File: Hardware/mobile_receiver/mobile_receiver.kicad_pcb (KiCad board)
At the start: 4 copper layers, 82.5 x 142 mm, 33 parts, among them J1 Conn_02x07_Top_Bottom, SW1 SW_SPST, SW2 SW_Push, SW3 SW_Push, SW4 SW_Push, SW5 SW_Push, SW6 SW_Push, SW7 SW_Push, U2 kb2040

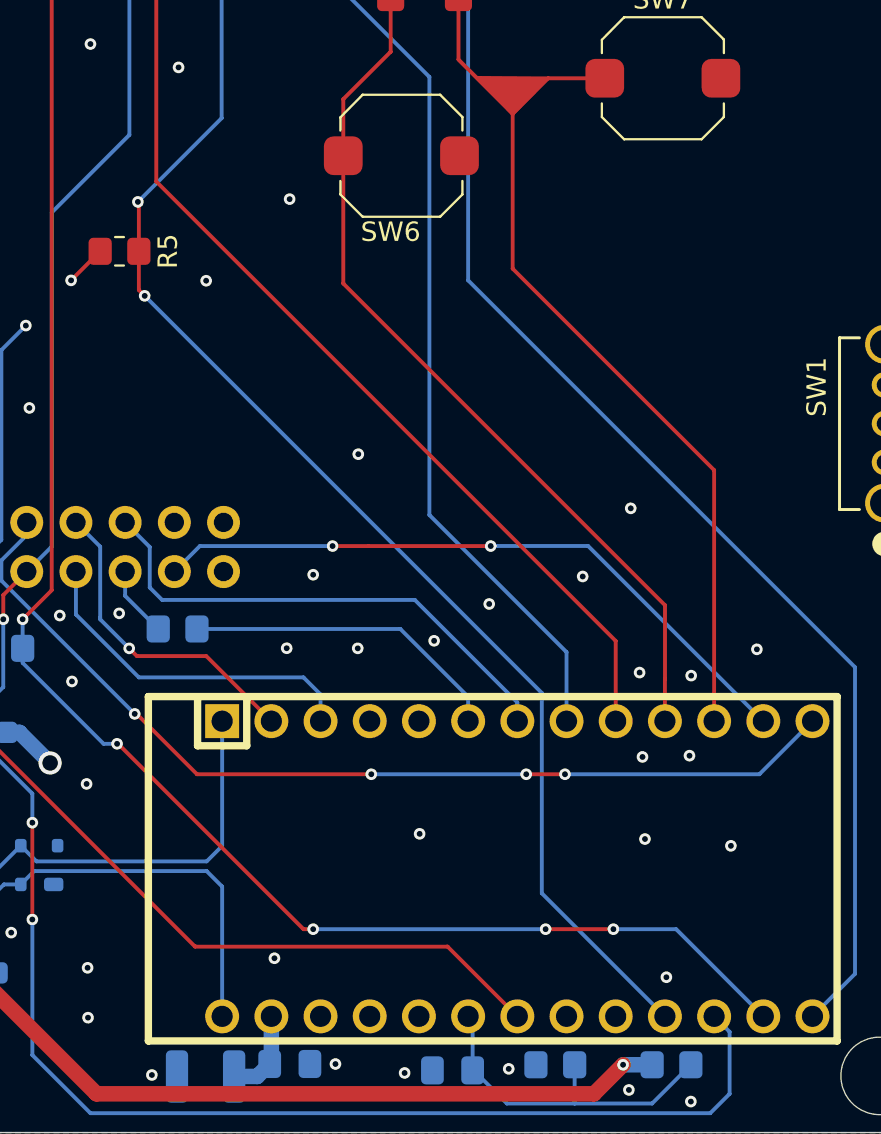
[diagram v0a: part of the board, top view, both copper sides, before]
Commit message: Vias and trace spacing
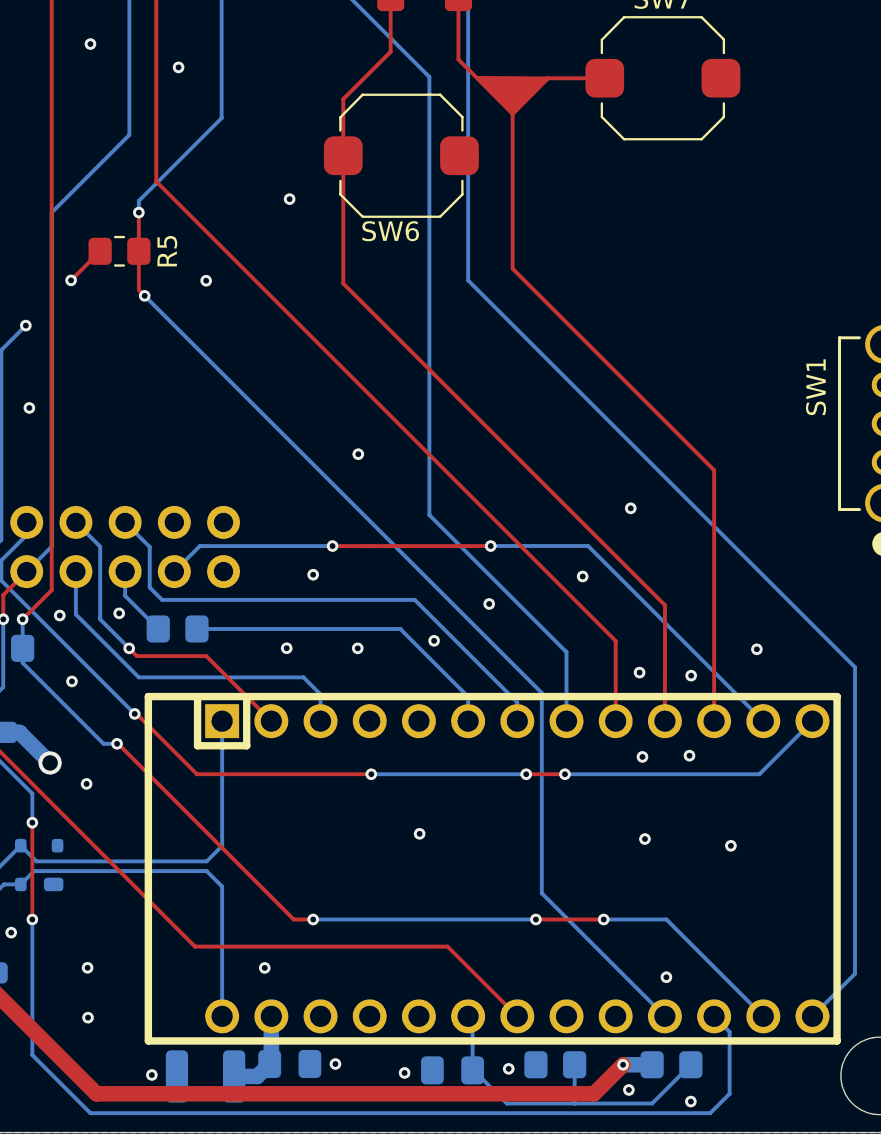
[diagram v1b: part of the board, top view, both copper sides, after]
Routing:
- added copper zone on In1.Cu, net GND
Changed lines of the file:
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@@
 	)
 	(via
-		(at 214.5 213)
+		(at 214 213.5)
 		(size 0.6)
 		(drill 0.3)
@@
 	)
 	(segment
-		(start 216 211.5)
-		(end 206.43 201.93)
+		(start 206.43 201.93)
+		(end 206.375 201.93)
+		(width 0.2)
+		(layer "F.Cu")
+		(net 18)
+	)
+	(segment
+		(start 231.5 211)
+		(end 228 211)
+		(width 0.2)
+		(layer "F.Cu")
+		(net 18)
+	)
+	(segment
+		(start 216.5 211)
+		(end 215.5 211)
 		(width 0.2)
 		(layer "F.Cu")
@@
 	)
 	(segment
-		(start 216.5 211.5)
-		(end 216 211.5)
+		(start 215.5 211)
+		(end 206.43 201.93)
 		(width 0.2)
 		(layer "F.Cu")
 		(net 18)
 	)
-	(segment
-		(start 206.43 201.93)
-		(end 206.375 201.93)
-		(width 0.2)
-		(layer "F.Cu")
+	(via
+		(at 231.5 211)
+		(size 0.6)
+		(drill 0.3)
+		(layers "F.Cu" "B.Cu")
 		(net 18)
 	)
-	(segment
-		(start 228.5 211.5)
-		(end 232 211.5)
-		(width 0.2)
-		(layer "F.Cu")
+	(via
+		(at 203 144)
+		(size 0.6)
+		(drill 0.3)
+		(layers "F.Cu" "B.Cu")
 		(net 18)
 	)
 	(via
-		(at 232 211.5)
+		(at 228 211)
 		(size 0.6)
 		(drill 0.3)
@@
 	)
 	(via
-		(at 203 144)
+		(at 201.5 195.5)
 		(size 0.6)
 		(drill 0.3)
@@
 	)
 	(via
-		(at 228.5 211.5)
-		(size 0.6)
-		(drill 0.3)
-		(layers "F.Cu" "B.Cu")
-		(net 18)
-	)
-	(via
-		(at 201.5 195.5)
-		(size 0.6)
-		(drill 0.3)
-		(layers "F.Cu" "B.Cu")
-		(net 18)
-	)
-	(via
-		(at 216.5 211.5)
+		(at 216.5 211)
 		(size 0.6)
 		(drill 0.3)
@@
 	)
 	(segment
-		(start 216.5 211.5)
-		(end 228.5 211.5)
-		(width 0.2)
-		(layer "B.Cu")
-		(net 18)
-	)
-	(segment
-		(start 232 211.5)
-		(end 235.24 211.5)
-		(width 0.2)
-		(layer "B.Cu")
-		(net 18)
-	)
-	(segment
 		(start 201.5 197)
 		(end 201.5 195.5)
@@
 	)
 	(segment
-		(start 235.24 211.5)
-		(end 239.74 216)
+		(start 228 211)
+		(end 216.5 211)
 		(width 0.2)
 		(layer "B.Cu")
@@
 	)
 	(segment
+		(start 234.74 211)
+		(end 239.74 216)
+		(width 0.2)
+		(layer "B.Cu")
+		(net 18)
+	)
+	(segment
 		(start 203 144)
 		(end 203 137.583047)
@@
 	)
 	(segment
+		(start 231.5 211)
+		(end 234.74 211)
+		(width 0.2)
+		(layer "B.Cu")
+		(net 18)
+	)
+	(segment
 		(start 207.5 178.5)
 		(end 207.5 176.5)
@@
 	)
 	(segment
-		(start 207.45 173.95)
-		(end 207.5 174)
+		(start 207.5 174.5)
+		(end 207.5 176.5)
 		(width 0.2)
 		(layer "F.Cu")
@@
 		(net 19)
 	)
-	(segment
-		(start 207.5 174)
-		(end 207.5 176.5)
-		(width 0.2)
-		(layer "F.Cu")
+	(via
+		(at 207.8 178.8)
+		(size 0.6)
+		(drill 0.3)
+		(layers "F.Cu" "B.Cu")
 		(net 19)
 	)
 	(via
-		(at 207.8 178.8)
+		(at 207.5 174.5)
 		(size 0.6)
 		(drill 0.3)
@@
 		(net 19)
 	)
-	(via
-		(at 207.45 173.95)
-		(size 0.6)
-		(drill 0.3)
-		(layers "F.Cu" "B.Cu")
+	(segment
+		(start 207.5 174.5)
+		(end 207.5 173.9)
+		(width 0.2)
+		(layer "B.Cu")
 		(net 19)
 	)
@@
 	)
 	(segment
+		(start 228.304781 209.644781)
+		(end 234.66 216)
+		(width 0.2)
+		(layer "B.Cu")
+		(net 19)
+	)
+	(segment
+		(start 207.5 173.9)
+		(end 211.774427 169.625573)
+		(width 0.2)
+		(layer "B.Cu")
+		(net 19)
+	)
+	(segment
+		(start 211.774427 133.88862)
+		(end 212.884427 132.77862)
+		(width 0.2)
+		(layer "B.Cu")
+		(net 19)
+	)
+	(segment
 		(start 211.774427 169.625573)
 		(end 211.774427 133.88862)
-		(width 0.2)
-		(layer "B.Cu")
-		(net 19)
-	)
-	(segment
-		(start 228.304781 209.644781)
-		(end 234.66 216)
-		(width 0.2)
-		(layer "B.Cu")
-		(net 19)
-	)
-	(segment
-		(start 211.774427 133.88862)
-		(end 212.884427 132.77862)
-		(width 0.2)
-		(layer "B.Cu")
-		(net 19)
-	)
-	(segment
-		(start 207.45 173.95)
-		(end 211.774427 169.625573)
 		(width 0.2)
 		(layer "B.Cu")
@@
 		(connect_pads
 			(clearance 0.5)
+		)
+		(min_thickness 0.25)
+		(filled_areas_thickness no)
+		(fill yes
+			(thermal_gap 0.5)
+			(thermal_bridge_width 0.5)
+		)
+		(polygon
+			(pts
+				(xy 166.5 80) (xy 249 80) (xy 249 222) (xy 166.5 222)
+			)
+		)
+	)
+	(zone
+		(net 1)
+		(net_name "GND")
+		(layer "In1.Cu")
+		(hatch edge 0.5)
+		(connect_pads
+			(clearance 0.5)

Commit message: Saved the previous update in kicad
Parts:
- C3, C6: footprint Capacitor_SMD:C_1210_3225Metric -> Capacitor_SMD:C_0805_2012Metric_Pad1.18x1.45mm_HandSolder
- moved C3 0.46 mm to (192.5, 194.0)
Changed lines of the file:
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@@
 		)
 	)
-	(footprint "Capacitor_SMD:C_1210_3225Metric"
+	(footprint "Capacitor_SMD:C_0805_2012Metric_Pad1.18x1.45mm_HandSolder"
 		(layer "B.Cu")
-		(at 192.5 194.5 90)
-		(descr "Capacitor SMD 1210 (3225 Metric), square (rectangular) end terminal, IPC-7351 nominal, (Body size source: IPC-SM-782 page 76, https://www.pcb-3d.com/wordpress/wp-content/uploads/ipc-sm-782a_amendment_1_and_2.pdf), generated with kicad-footprint-generator")
-		(tags "capacitor")
+		(at 192.5 194.0375 90)
+		(descr "Capacitor SMD 0805 (2012 Metric), square (rectangular) end terminal, IPC-7351 nominal with elongated pad for handsoldering. (Body size source: IPC-SM-782 page 76, https://www.pcb-3d.com/wordpress/wp-content/uploads/ipc-sm-782a_amendment_1_and_2.pdf, https://docs.google.com/spreadsheets/d/1BsfQQcO9C6DZCsRaXUlFlo91Tg2WpOkGARC1WS5S8t0/edit?usp=sharing), generated with kicad-footprint-generator")
+		(tags "capacitor handsolder")
 		(property "Reference" "C3"
-			(at 0 -2.5 270)
+			(at -0.4625 1.68 270)
 			(layer "B.SilkS")
 			(effects
@@
 		)
 		(property "Value" "10uF"
-			(at 0 -2.3 90)
+			(at 0 -1.68 270)
 			(layer "B.Fab")
 			(effects
@@
 		)
 		(property "Datasheet" "~"
-			(at 0 0 90)
+			(at 0 0 270)
 			(layer "B.Fab")
 			(hide yes)
@@
 		)
 		(property "Description" "Unpolarized capacitor"
-			(at 0 0 90)
+			(at 0 0 270)
 			(layer "B.Fab")
 			(hide yes)
@@
 		(attr smd)
 		(fp_line
-			(start -0.711252 -1.36)
-			(end 0.711252 -1.36)
+			(start -0.261252 -0.735)
+			(end 0.261252 -0.735)
 			(stroke
 				(width 0.12)
@@
 		)
 		(fp_line
-			(start -0.711252 1.36)
-			(end 0.711252 1.36)
+			(start -0.261252 0.735)
+			(end 0.261252 0.735)
 			(stroke
 				(width 0.12)
@@
 		)
 		(fp_rect
-			(start -2.3 1.6)
-			(end 2.3 -1.6)
+			(start -1.88 0.98)
+			(end 1.88 -0.98)
 			(stroke
 				(width 0.05)
@@
 		)
 		(fp_rect
-			(start -1.6 1.25)
-			(end 1.6 -1.25)
+			(start -1 0.625)
+			(end 1 -0.625)
 			(stroke
 				(width 0.1)
@@
 		)
 		(fp_text user "${REFERENCE}"
-			(at 0 0 90)
+			(at 0 0 270)
 			(layer "B.Fab")
 			(effects
 				(font
-					(size 0.8 0.8)
-					(thickness 0.12)
+					(size 0.5 0.5)
+					(thickness 0.08)
 				)
 				(justify mirror)
@@
 		)
 		(pad "1" smd roundrect
-			(at -1.475 0 90)
-			(size 1.15 2.7)
+			(at -1.0375 0 90)
+			(size 1.175 1.45)
 			(layers "B.Cu" "B.Mask" "B.Paste")
-			(roundrect_rratio 0.217391)
+			(roundrect_rratio 0.212766)
 			(net 1 "GND")
 			(pintype "passive")
 		)
 		(pad "2" smd roundrect
-			(at 1.475 0 90)
-			(size 1.15 2.7)
+			(at 1.0375 0 90)
+			(size 1.175 1.45)
 			(layers "B.Cu" "B.Mask" "B.Paste")
-			(roundrect_rratio 0.217391)
+			(roundrect_rratio 0.212766)
 			(net 34 "+3.3V")
 			(pintype "passive")
 		)
 		(embedded_fonts no)
-		(model "${KICAD9_3DMODEL_DIR}/Capacitor_SMD.3dshapes/C_1210_3225Metric.step"
+		(model "${KICAD9_3DMODEL_DIR}/Capacitor_SMD.3dshapes/C_0805_2012Metric.step"
 			(offset
 				(xyz 0 0 0)
@@
 		)
 	)
-	(footprint "Capacitor_SMD:C_1210_3225Metric"
+	(footprint "Capacitor_SMD:C_0805_2012Metric_Pad1.18x1.45mm_HandSolder"
 		(layer "B.Cu")
 		(at 210.942559 219.105205 180)
-		(descr "Capacitor SMD 1210 (3225 Metric), square (rectangular) end terminal, IPC-7351 nominal, (Body size source: IPC-SM-782 page 76, https://www.pcb-3d.com/wordpress/wp-content/uploads/ipc-sm-782a_amendment_1_and_2.pdf), generated with kicad-footprint-generator")
-		(tags "capacitor")
+		(descr "Capacitor SMD 0805 (2012 Metric), square (rectangular) end terminal, IPC-7351 nominal with elongated pad for handsoldering. (Body size source: IPC-SM-782 page 76, https://www.pcb-3d.com/wordpress/wp-content/uploads/ipc-sm-782a_amendment_1_and_2.pdf, https://docs.google.com/spreadsheets/d/1BsfQQcO9C6DZCsRaXUlFlo91Tg2WpOkGARC1WS5S8t0/edit?usp=sharing), generated with kicad-footprint-generator")
+		(tags "capacitor handsolder")
 		(property "Reference" "C6"
-			(at 4.442559 0.105205 0)
+			(at 0 1.68 0)
 			(layer "B.SilkS")
 			(effects
@@
 		)
 		(property "Value" "4.7µF"
-			(at 0 -2.3 0)
+			(at 0 -1.68 0)
 			(layer "B.Fab")
-			(hide yes)
 			(effects
 				(font
@@
 		(attr smd)
 		(fp_line
-			(start -0.711252 1.36)
-			(end 0.711252 1.36)
+			(start -0.261252 0.735)
+			(end 0.261252 0.735)
 			(stroke
 				(width 0.12)
@@
 		)
 		(fp_line
-			(start -0.711252 -1.36)
-			(end 0.711252 -1.36)
+			(start -0.261252 -0.735)
+			(end 0.261252 -0.735)
 			(stroke
 				(width 0.12)
@@
 		)
 		(fp_rect
-			(start -2.3 1.6)
-			(end 2.3 -1.6)
+			(start -1.88 0.98)
+			(end 1.88 -0.98)
 			(stroke
 				(width 0.05)
@@
 		)
 		(fp_rect
-			(start -1.6 1.25)
-			(end 1.6 -1.25)
+			(start -1 0.625)
+			(end 1 -0.625)
 			(stroke
 				(width 0.1)
@@
 			(effects
 				(font
-					(size 0.8 0.8)
-					(thickness 0.12)
+					(size 0.5 0.5)
+					(thickness 0.08)
 				)
 				(justify mirror)
@@
 		)
 		(pad "1" smd roundrect
-			(at -1.475 0 180)
-			(size 1.15 2.7)
+			(at -1.0375 0 180)
+			(size 1.175 1.45)
 			(layers "B.Cu" "B.Mask" "B.Paste")
-			(roundrect_rratio 0.217391)
+			(roundrect_rratio 0.212766)
 			(net 4 "/SYS_VBUS")
 			(pintype "passive")
 		)
 		(pad "2" smd roundrect
-			(at 1.475 0 180)
-			(size 1.15 2.7)
+			(at 1.0375 0 180)
+			(size 1.175 1.45)
 			(layers "B.Cu" "B.Mask" "B.Paste")
-			(roundrect_rratio 0.217391)
+			(roundrect_rratio 0.212766)
 			(net 1 "GND")
 			(pintype "passive")
 		)
 		(embedded_fonts no)
-		(model "${KICAD9_3DMODEL_DIR}/Capacitor_SMD.3dshapes/C_1210_3225Metric.step"
+		(model "${KICAD9_3DMODEL_DIR}/Capacitor_SMD.3dshapes/C_0805_2012Metric.step"
 			(offset
 				(xyz 0 0 0)
@@
 	)
 	(via
-		(at 230.41493 193.289583)
+		(at 227.960154 189.922244)
 		(size 0.6)
 		(drill 0.3)
@@
 	)
 	(segment
-		(start 216 198.5)
-		(end 216.88 199.38)
+		(start 216.88 199.38)
+		(end 216.88 200.76)
 		(width 0.2)
 		(layer "B.Cu")
@@
 	)
 	(segment
-		(start 204.250805 195.250805)
-		(end 207.5 198.5)
+		(start 204.250805 195.599068)
+		(end 207.510509 198.858772)
 		(width 0.2)
 		(layer "B.Cu")
@@
 	)
 	(segment
-		(start 207.5 198.5)
-		(end 216 198.5)
+		(start 216.358772 198.858772)
+		(end 216.88 199.38)
 		(width 0.2)
 		(layer "B.Cu")
@@
 	)
 	(segment
-		(start 204.250805 193.037019)
-		(end 204.250805 195.250805)
+		(start 207.510509 198.858772)
+		(end 216.358772 198.858772)
 		(width 0.2)
 		(layer "B.Cu")
@@
 	)
 	(segment
-		(start 216.88 199.38)
-		(end 216.88 200.76)
+		(start 204.250805 193.037019)
+		(end 204.250805 195.599068)
 		(width 0.2)
 		(layer "B.Cu")
@@
 	)
 	(segment
-		(start 232.12 200.76)
-		(end 232.12 196.62)
+		(start 208.4 135.914193)
+		(end 205.264427 132.77862)
 		(width 0.2)
 		(layer "F.Cu")
@@
 	)
 	(segment
-		(start 208.4 135.914193)
-		(end 205.264427 132.77862)
+		(start 232.12 200.76)
+		(end 232.12 195.951903)
 		(width 0.2)
 		(layer "F.Cu")
@@
 	)
 	(segment
-		(start 208.4 172.9)
-		(end 208.4 135.914193)
+		(start 232.12 195.951903)
+		(end 208.4 172.231903)
 		(width 0.2)
 		(layer "F.Cu")
@@
 	)
 	(segment
-		(start 232.12 196.62)
-		(end 208.4 172.9)
+		(start 208.4 172.231903)
+		(end 208.4 135.914193)
 		(width 0.2)
 		(layer "F.Cu")

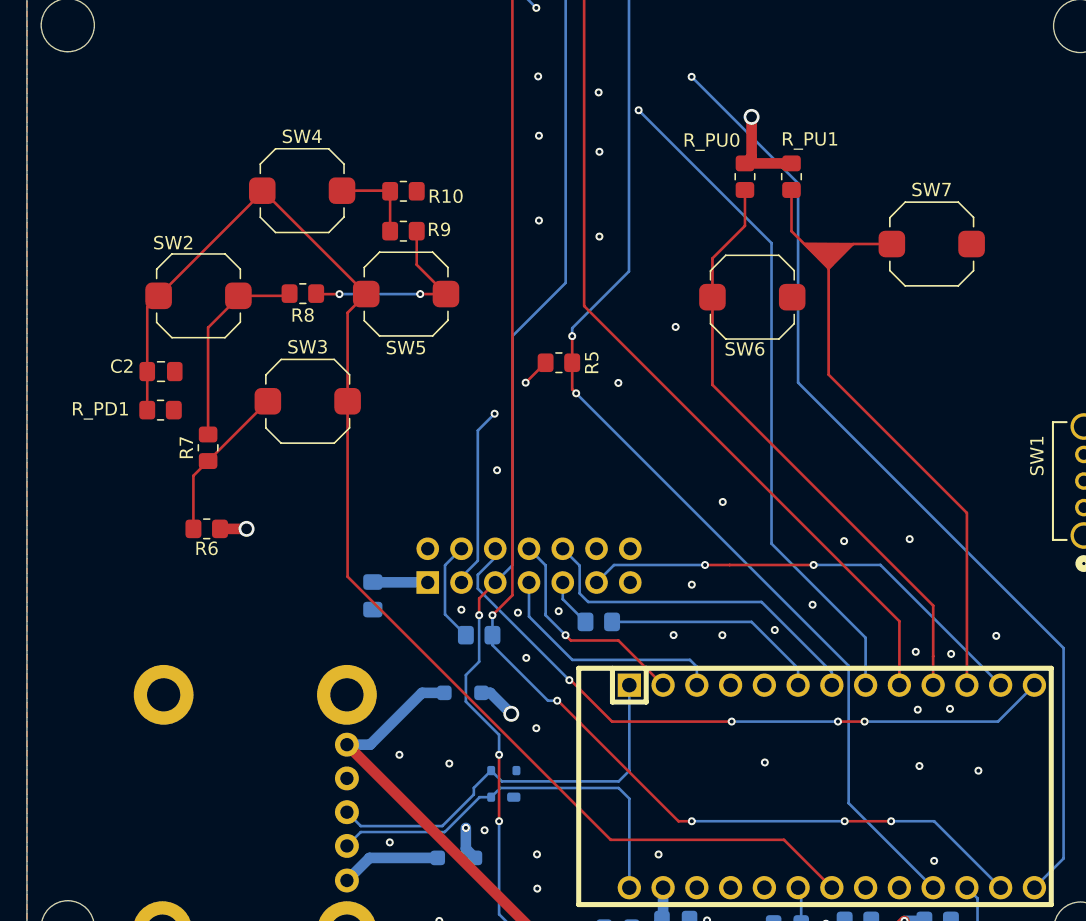
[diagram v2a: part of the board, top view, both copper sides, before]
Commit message: Updated traces and vias according to new switches and passives
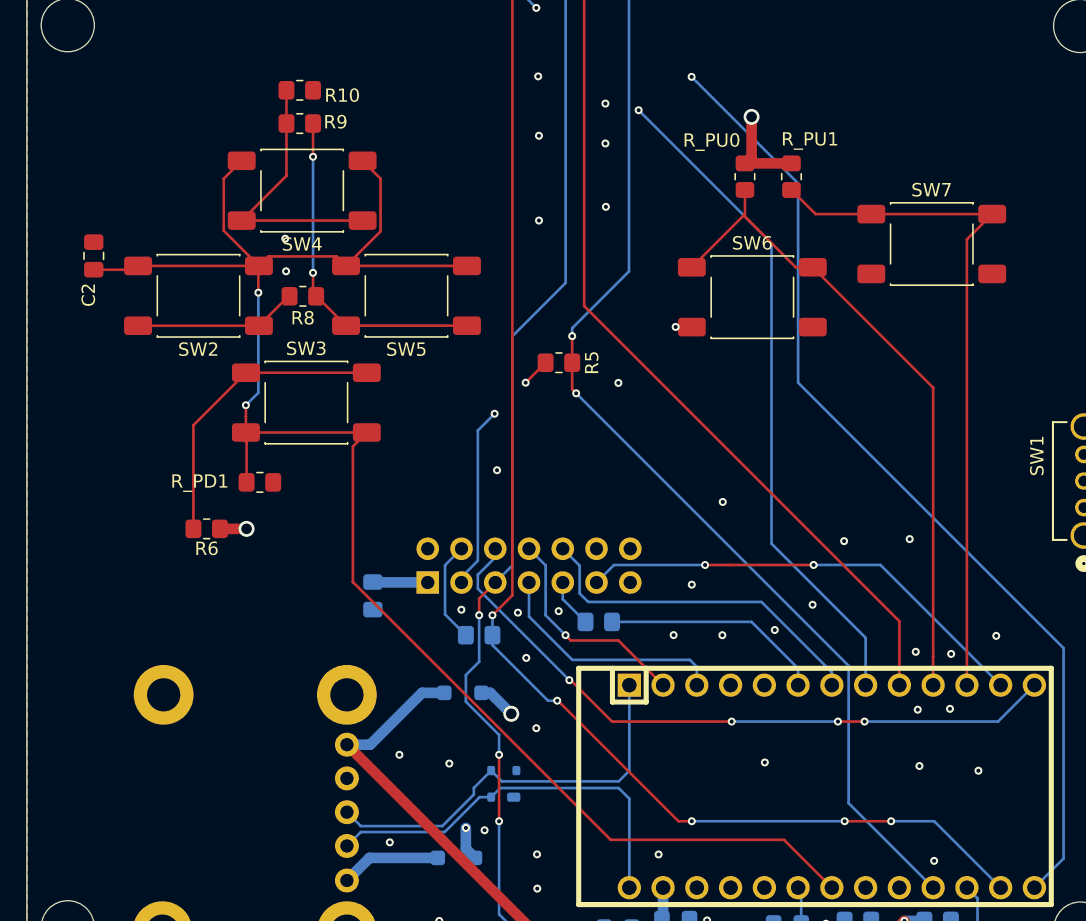
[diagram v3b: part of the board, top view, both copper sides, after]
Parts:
- removed R7: 10K, Resistor_SMD:R_0805_2012Metric_Pad1.20x1.40mm_HandSolder
- SW2, SW3, SW4, SW5, SW6, SW7: footprint Button_Switch_SMD:SW_Push_1TS009xxxx-xxxx-xxxx_6x6x5mm -> Button_Switch_SMD:SW_Push_1P1T_NO_E-Switch_TL3301NxxxxxG
- moved R9 11.2 mm to (187.0, 158.5)
- moved R10 10.9 mm to (187.0, 156.0)
- moved C2 10.1 mm to (171.5, 168.5), turned to 90 degrees
- moved R_PD1 9.24 mm to (184.0, 185.5)
- moved R8 0.20 mm to (187.2, 171.5)
- moved SW3 0.14 mm to (187.5, 179.5)
- moved SW5 0.13 mm to (195.0, 171.5)
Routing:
- net /DPAD_ADC: track 99.6 -> 131.5 mm, vias 0 -> 2
- net Net-(R10-Pad2): track 6.64 -> 20.8 mm
- net Net-(R6-Pad1): track 12.3 -> 22.5 mm
- net Net-(R8-Pad1): track 15.5 -> 25.4 mm
- net /BTN_A: track 45.2 -> 49.5 mm
- net /BTN_B: track 48.2 -> 52.1 mm
- net Net-(R7-Pad1): track 15.5 -> 12.3 mm
- net GND: vias 47 -> 49
